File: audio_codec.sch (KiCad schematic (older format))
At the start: 13 parts

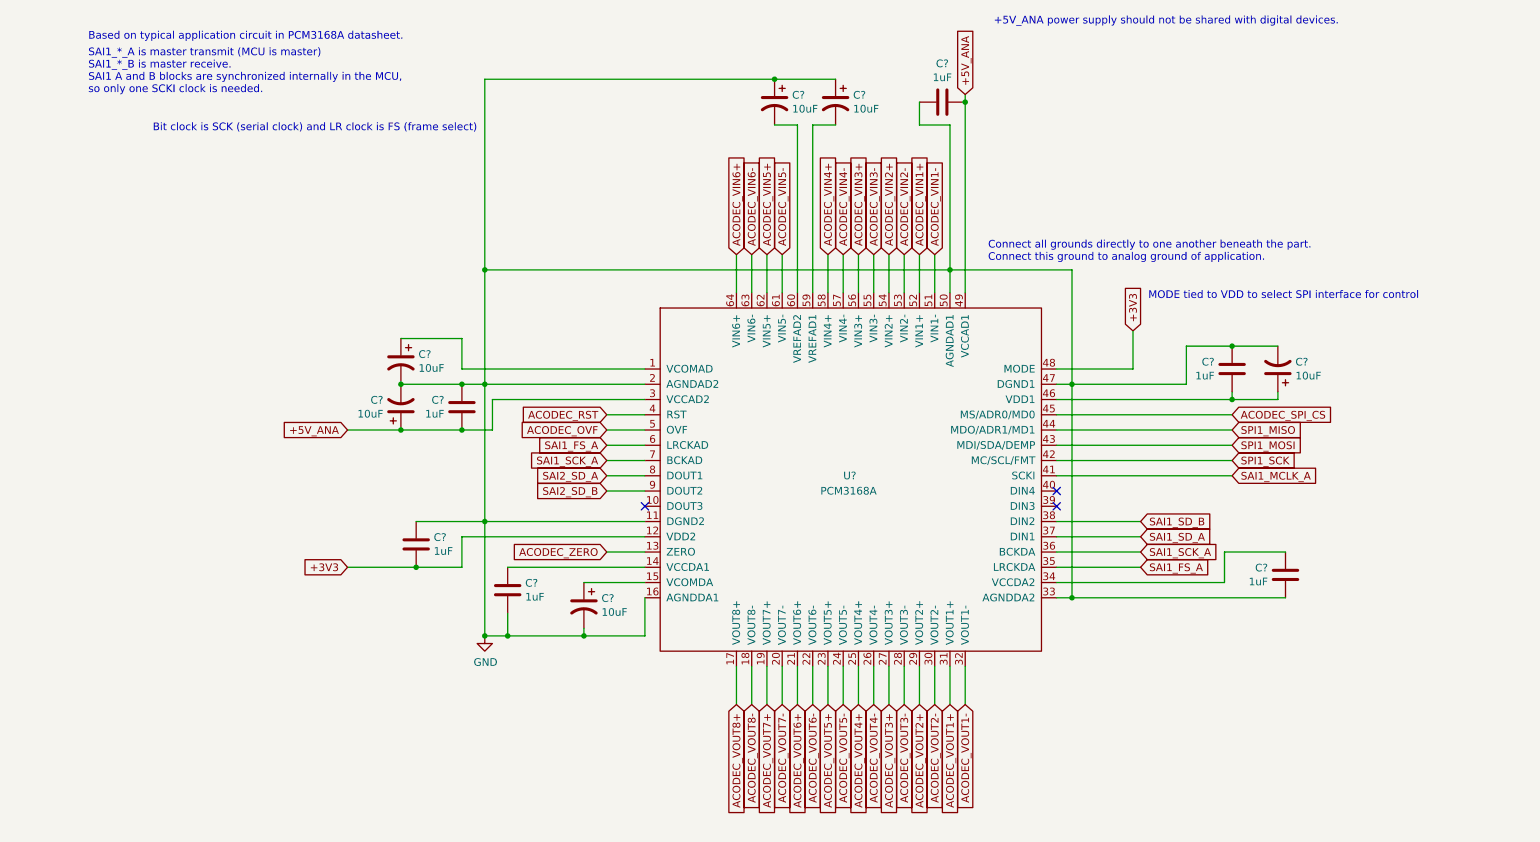
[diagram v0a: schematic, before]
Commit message: First proposed pin layout of SODIMM connector
Will need to add GPIO / ADC pins as needed, but let's wait to see if we don't
need to use more pins.

Double-checked and fixed CODEC and MCU's power supply.
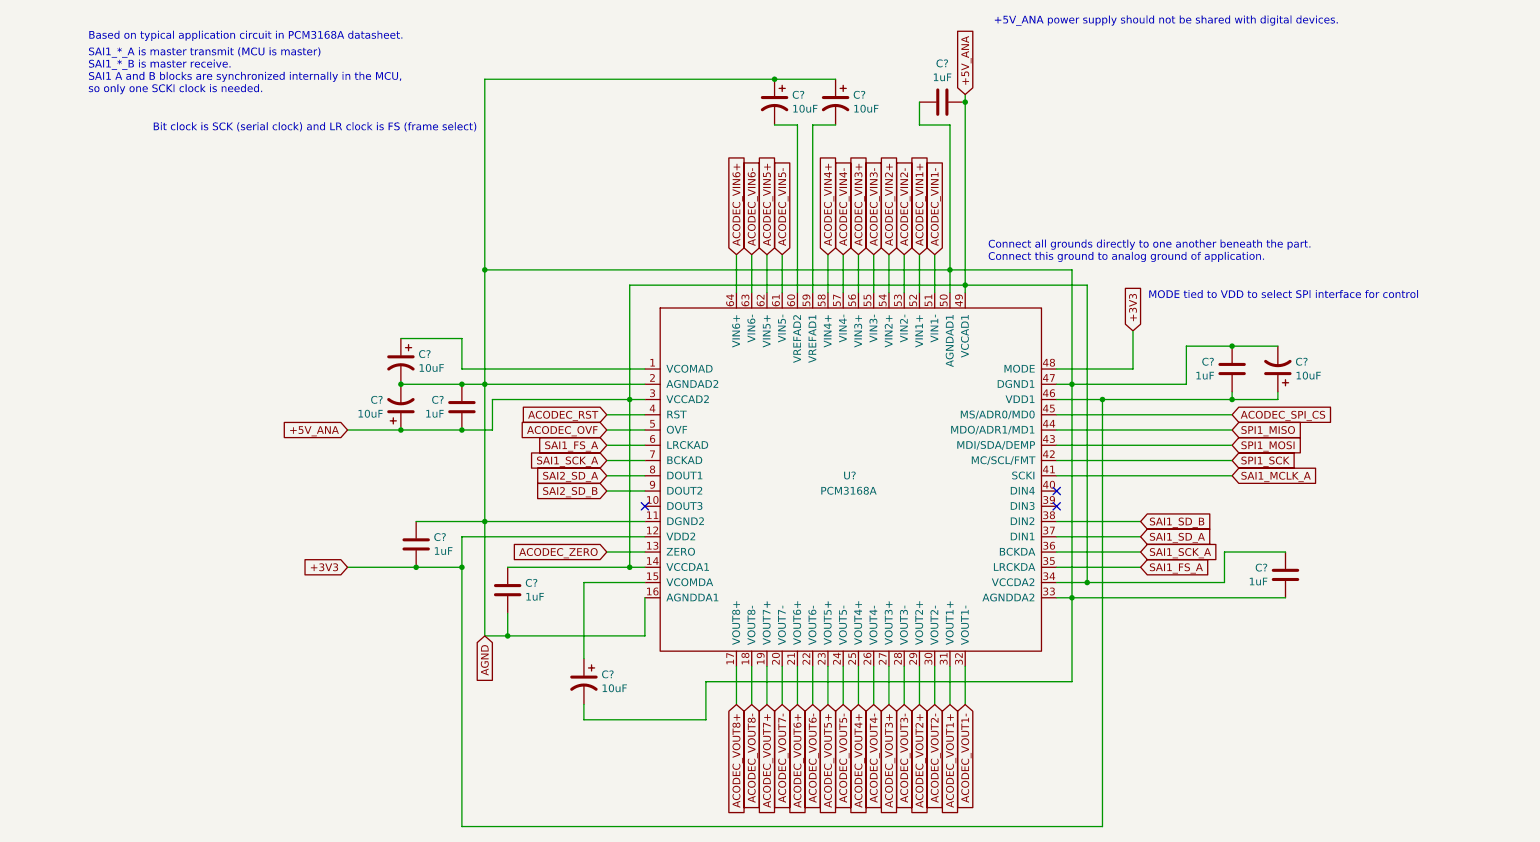
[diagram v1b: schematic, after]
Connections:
- net +3V3: now also C?.1, C?.2, U?.46 (VDD1)
- net +5V_ANA: now also C?.1, C?.1, U?.14 (VCCDA1), U?.34 (VCCDA2)
- net GND renamed AGND
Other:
- moved on the sheet: C?
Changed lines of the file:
@@
 $Descr A4 11693 8268
 encoding utf-8
-Sheet 6 12
+Sheet 6 13
 Title ""
 Date ""
@@
 	3300 3250 3300 3050
 Wire Wire Line
-	3300 3050 4300 3050
+	3300 3050 4200 3050
 Wire Wire Line
 	2700 3250 2350 3250
@@
 	-1   0    0    -1
 $EndComp
-Wire Wire Line
-	2350 4150 2800 4150
 Text GLabel 6400 1050 1    50   Input ~ 0
 +5V_ANA
@@
 L Device:CP1 C?
 U 1 1 5CF79200
-P 3900 4400
-F 0 "C?" H 3785 4446 50  0000 R CNN
-F 1 "10uF" H 3785 4355 50  0000 R CNN
-F 2 "" H 3900 4400 50  0001 C CNN
-F 3 "~" H 3900 4400 50  0001 C CNN
-	1    3900 4400
+P 3900 4900
+F 0 "C?" H 3785 4946 50  0000 R CNN
+F 1 "10uF" H 3785 4855 50  0000 R CNN
+F 2 "" H 3900 4900 50  0001 C CNN
+F 3 "~" H 3900 4900 50  0001 C CNN
+	1    3900 4900
 	-1   0    0    -1
 $EndComp
@@
 	8100 4050 8100 4250
 Wire Wire Line
-	8100 4250 7000 4250
+	8100 4250 7200 4250
 $Comp
 L Device:C C?
@@
 	3900 4250 4300 4250
 Wire Wire Line
-	4300 4600 3900 4600
-Wire Wire Line
-	3900 4600 3900 4550
-Wire Wire Line
-	4300 4150 3400 4150
+	4300 4150 4200 4150
 Wire Wire Line
 	3400 4450 3400 4600
-Wire Wire Line
-	3400 4600 3900 4600
-Connection ~ 3900 4600
 Text GLabel 8150 3250 2    50   Input ~ 0
 SPI1_MISO
@@
 Wire Wire Line
 	3250 2950 3250 2200
-Wire Wire Line
-	3250 2200 6300 2200
 Connection ~ 6300 2200
 Wire Wire Line
@@
 	7100 2200 7100 2950
 Connection ~ 7100 4350
-Wire Wire Line
-	7100 4350 8500 4350
 Wire Wire Line
 	7000 2950 7100 2950
@@
 $EndComp
 Wire Wire Line
-	7000 3050 8150 3050
+	7000 3050 7300 3050
 Wire Wire Line
 	8150 3050 8150 3000
@@
 NoConn ~ 4300 3750
 Wire Wire Line
-	5300 1250 5300 2350
-Wire Wire Line
-	5400 1250 5400 2350
-$Comp
-L power:GND #PWR?
-U 1 1 5CF95CCF
-P 3250 4600
-F 0 "#PWR?" H 3250 4350 50  0001 C CNN
-F 1 "GND" H 3255 4427 50  0000 C CNN
-F 2 "" H 3250 4600 50  0001 C CNN
-F 3 "" H 3250 4600 50  0001 C CNN
-	1    3250 4600
-	1    0    0    -1
-$EndComp
-Connection ~ 3250 4600
+	5300 1250 5300 2200
 Wire Wire Line
 	5550 950  5150 950
@@
 ACODEC_VIN1-
 Wire Wire Line
-	6400 1100 6400 2350
+	6400 1100 6400 2300
 Wire Wire Line
 	6100 1100 6100 1250
@@
 	6400 1050 6400 1100
 Connection ~ 6400 1100
+Wire Wire Line
+	7300 3050 7300 5850
+Wire Wire Line
+	7300 5850 3100 5850
+Wire Wire Line
+	3100 5850 3100 4150
+Connection ~ 7300 3050
+Wire Wire Line
+	7300 3050 8150 3050
+Connection ~ 3100 4150
+Wire Wire Line
+	4200 2300 4200 3050
+Connection ~ 6400 2300
+Wire Wire Line
+	6400 2300 6400 2350
+Connection ~ 4200 3050
+Wire Wire Line
+	4200 3050 4300 3050
+Wire Wire Line
+	4200 3050 4200 4150
+Connection ~ 4200 4150
+Wire Wire Line
+	4200 4150 3400 4150
+Wire Wire Line
+	7200 4250 7200 2300
+Wire Wire Line
+	7200 2300 6400 2300
+Connection ~ 7200 4250
+Wire Wire Line
+	7200 4250 7000 4250
+Wire Wire Line
+	5400 2300 4200 2300
+Wire Wire Line
+	5300 2200 5300 2350
+Wire Wire Line
+	6400 2300 5400 2300
+Wire Wire Line
+	5400 1250 5400 2200
+Wire Wire Line
+	5400 2200 5400 2350
+Wire Wire Line
+	3250 2200 6300 2200
+Wire Wire Line
+	3400 4600 4300 4600
+Wire Wire Line
+	3900 4250 3900 4750
+Wire Wire Line
+	3900 5050 3900 5150
+Wire Wire Line
+	3900 5150 4700 5150
+Wire Wire Line
+	4700 5150 4700 4900
+Wire Wire Line
+	4700 4900 7100 4900
+Wire Wire Line
+	7100 4350 8500 4350
+Wire Wire Line
+	7100 4350 7100 4900
+Wire Wire Line
+	2350 4150 2800 4150
+Text GLabel 3250 4600 3    50   Input ~ 0
+AGND
 $EndSCHEMATC
